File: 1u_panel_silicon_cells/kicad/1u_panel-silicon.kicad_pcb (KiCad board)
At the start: 2 copper layers, 83 x 100 mm, 134 parts, among them J1 MMS-104-01-[F/L]-SH, J2 2-1734592-0, Q1 DMP3050LVT-7, Q2 DMP2240UDM-7, U1 TCAN330GDCNT, U10 TPS63060DSCR, U11 TMP101NA/3KSLOTTED, U12 LTC4412, U13 LTC4411, U14 LTC4411, U15 LTC4411, U16 LTC4411, U2 TMP101NA/3KSLOTTED, U3 LT1618EMSTRPBF, U4 INA226AIDGSR, U5 LTC4411, U6 LTC4411, U7 STM32F091CCT7, U8 LTC4411, U9 LTC4411, X1 ECS-160-10-36Q-ES-TR

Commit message: possibly ready for silicon panel design review?
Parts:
- U13, U14, U15, U16, U5, U6, U8, U9: moved to F.Cu
- moved U14 127.2 mm to (179.8, 119.2), turned to 0 degrees
- moved U15 118.5 mm to (171.2, 105.0), turned to 0 degrees
- moved R31 109.9 mm to (179.5, 116.0)
- moved U13 103.6 mm to (140.8, 117.9), turned to -90 degrees
- moved U8 96.9 mm to (161.0, 96.0)
- moved R32 96.1 mm to (172.2, 101.2)
- moved U16 92.0 mm to (140.5, 104.0)
- moved U9 89.0 mm to (123.1, 118.2), turned to -90 degrees
- moved R28 88.2 mm to (161.0, 98.2), turned to 180 degrees
- moved R30 81.9 mm to (144.5, 117.9), turned to -90 degrees
- moved U6 71.2 mm to (141.2, 89.2)
- moved U5 70.0 mm to (127.8, 92.8), turned to 90 degrees
- moved R29 69.9 mm to (125.8, 118.2), turned to -90 degrees
- moved R8 67.8 mm to (140.8, 91.5), turned to 180 degrees
- moved R33 67.4 mm to (140.5, 106.8), turned to 180 degrees
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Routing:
- net VSOLAR: track 48.2 -> 236.3 mm, vias 12 -> 30
- net Net-(J2-DEBUG-3): track 2.12 -> 89.1 mm
- net Net-(J2-DEBUG-2): track 2.29 -> 88.2 mm
- net Net-(J2-DEBUG-1): track 7.16 -> 92.4 mm
- net Net-(J2-DEBUG-0): track 2.49 -> 86.7 mm
- net Net-(J2-SWO): track 2.38 -> 86.0 mm
- net Net-(J2-VBUSP-Pad1): track 2.08 -> 72.6 mm
- net Net-(D7-A1): track 0.00 -> 17.2 mm, vias 0 -> 4
- net Net-(D8-A1): track 0.00 -> 10.9 mm, vias 0 -> 4
- net Net-(D11-A1): track 0.00 -> 10.6 mm, vias 0 -> 5
- net Net-(D13-A1): track 0.00 -> 7.34 mm, vias 0 -> 5
- net Net-(D12-A1): track 0.00 -> 3.49 mm, vias 0 -> 4
- net Net-(D2-A1): track 0.00 -> 2.98 mm, vias 0 -> 6
- net Net-(D10-A1): track 0.00 -> 2.93 mm, vias 0 -> 5
- net /1u_panel-microcontroller/SWCLK: track 66.0 -> 68.1 mm
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
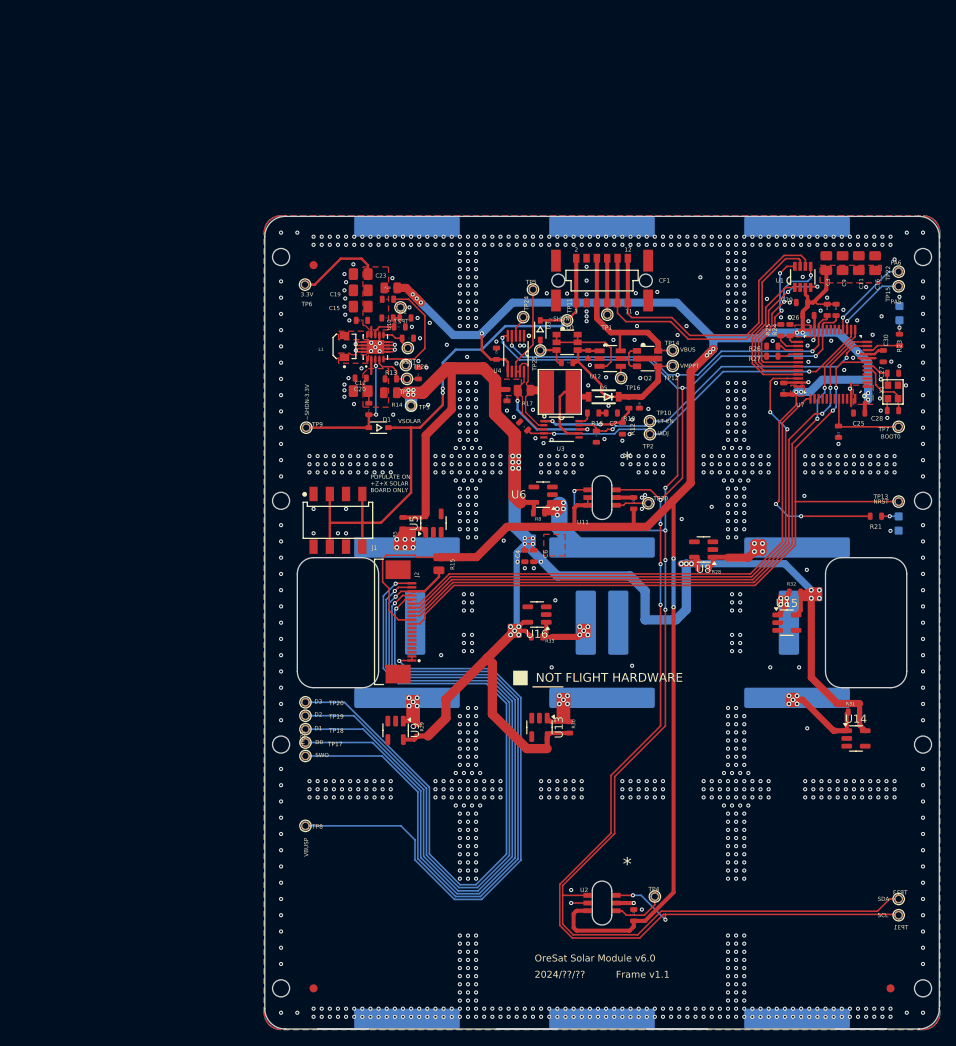
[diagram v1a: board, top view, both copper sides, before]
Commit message: fixed board outline, title blocks
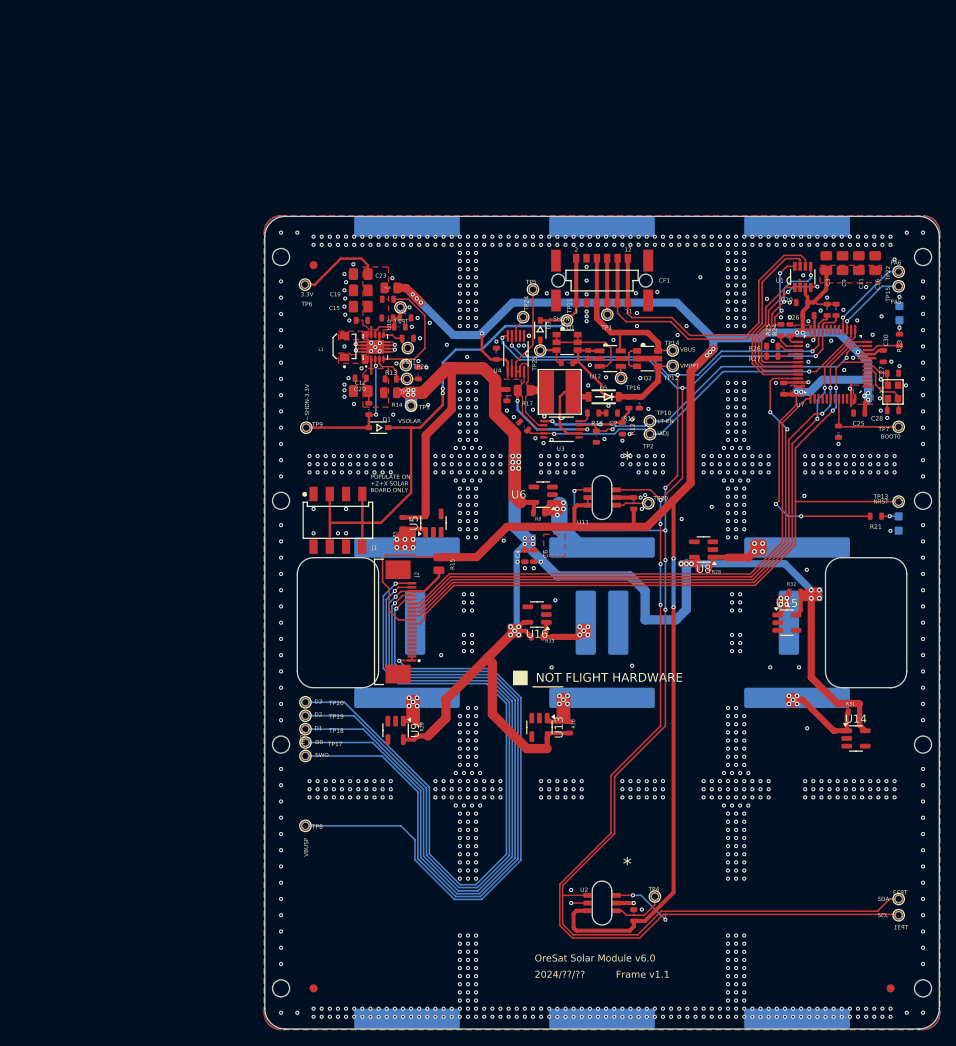
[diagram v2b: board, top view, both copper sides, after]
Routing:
- net GND: track 27.5 -> 31.4 mm
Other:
- outline, holes or cut-outs redrawn

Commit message: updating remote repo for design review
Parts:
- moved R31 0.50 mm to (179.5, 116.5)
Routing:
- net GND: track 31.4 -> 144.6 mm, vias 1180 -> 1202
- net /1u_panel-power/~{SHUTDOWN}: track 75.0 -> 73.1 mm
- net Net-(D11-A1): track 10.6 -> 10.1 mm
- net VSOLAR: track 236.3 -> 236.5 mm, vias 30 -> 28
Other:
- board text added: "2024/08/20"

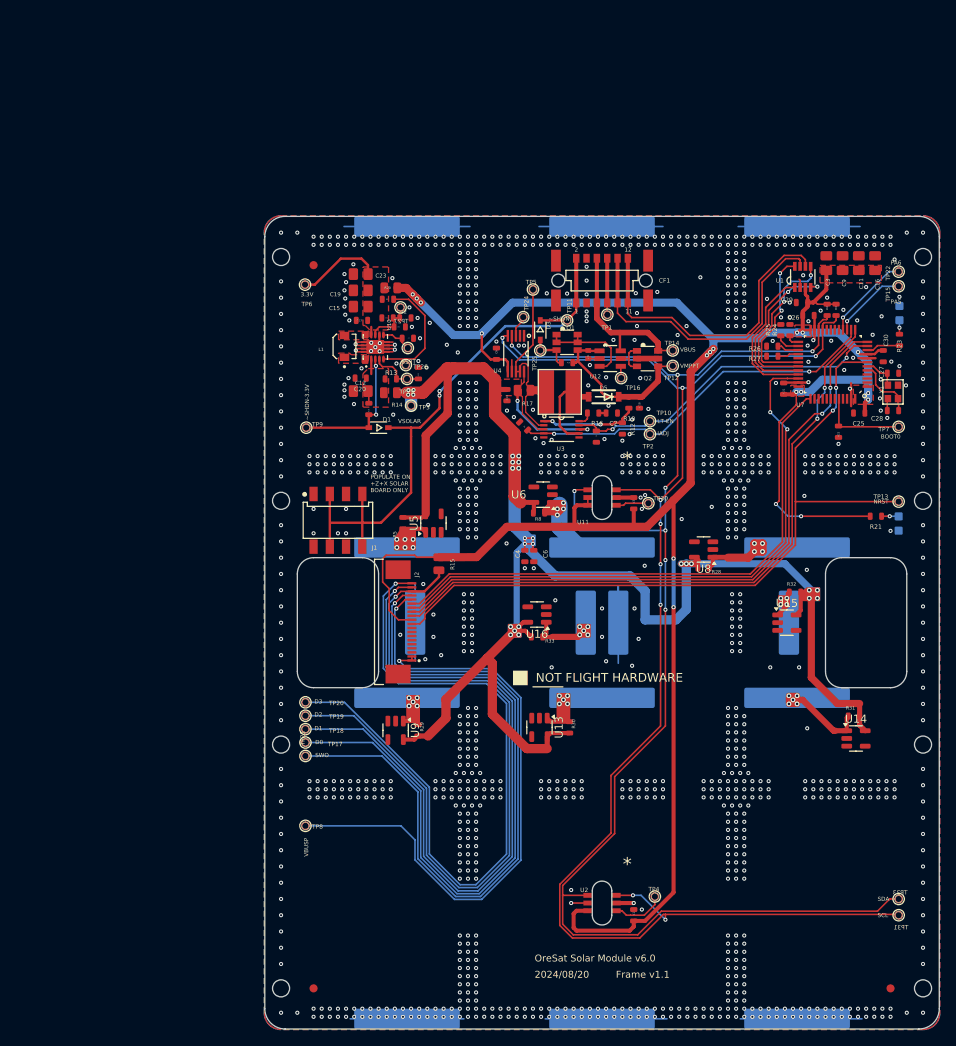
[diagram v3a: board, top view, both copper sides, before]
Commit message: commiting silicon solar panel before moving programming header
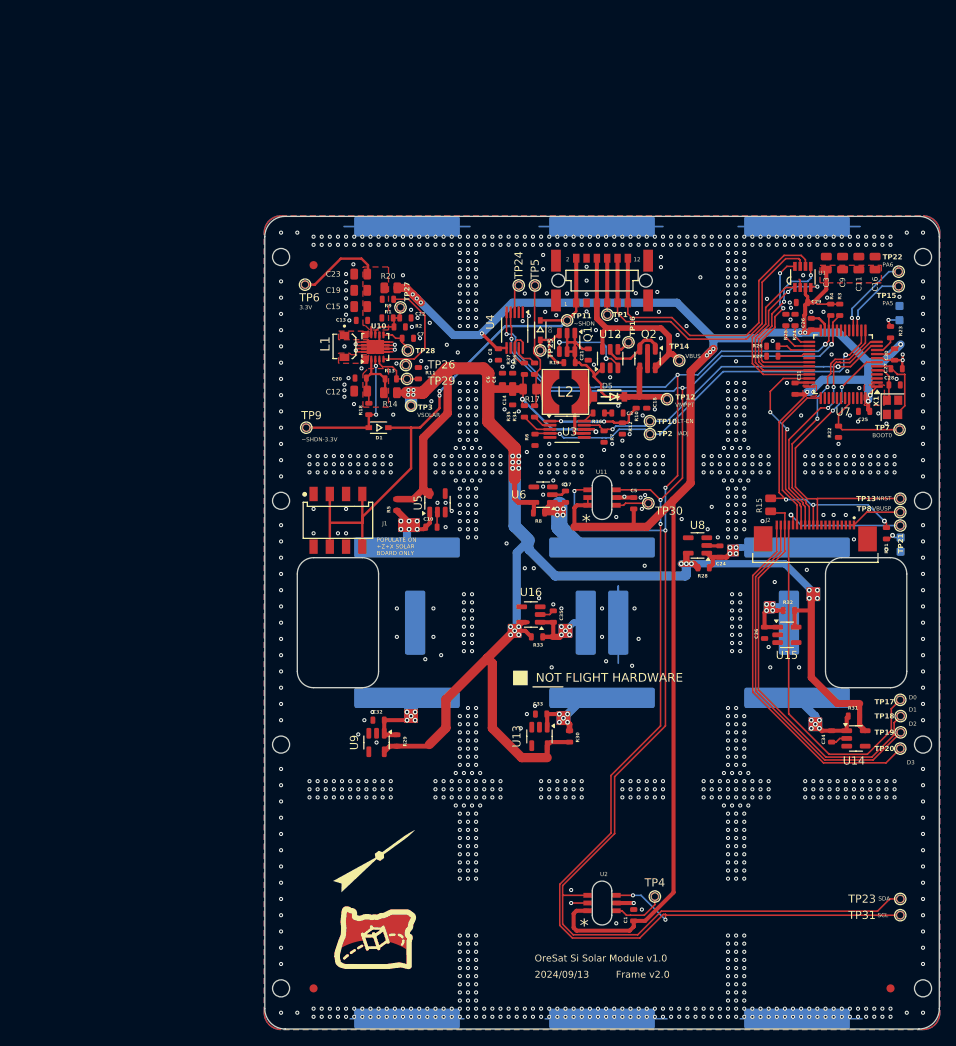
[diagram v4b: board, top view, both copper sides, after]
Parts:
- added C10: 1u, oresat-passives:0603-C-NOSILK, F.Cu at (127.5, 93.2)
- added C17: 1u, oresat-passives:0603-C-NOSILK, F.Cu at (144.0, 89.5)
- added C24: 1u, oresat-passives:0603-C-NOSILK, F.Cu at (163.0, 96.2)
- added C32: 1u, oresat-passives:0603-C-NOSILK, F.Cu at (121.0, 117.0)
- added C33: 1u, oresat-passives:0603-C-NOSILK, F.Cu at (141.0, 116.2)
- added C34: 1u, oresat-passives:0603-C-NOSILK, F.Cu at (176.8, 119.0)
- added C35: 1u, oresat-passives:0603-C-NOSILK, F.Cu at (142.5, 104.2)
- added C36: 1u, oresat-passives:0603-C-NOSILK, F.Cu at (168.5, 106.2)
- added LOGO1: , oresat-graphics:PSAS_LOGO_10X10, F.Cu at (120.8, 134.0)
- added R34: 100, oresat-passives:0603-C-NOSILK, F.Cu at (140.2, 79.0)
- added R35: 100, oresat-passives:0603-C-NOSILK, F.Cu at (138.9, 79.0)
- added R36: 100, oresat-passives:0603-C-NOSILK, F.Cu at (140.2, 73.8)
- added R37: 100, oresat-passives:0603-C-NOSILK, F.Cu at (138.9, 73.8)
- added REF**: logo-small, oresat-graphics:logo-small, F.Cu at (120.5, 143.5)
- C1, C13, C14, C18, C2, C20, C22, C25, C26, C27, C28, C29, C30, C31, C4, C5, C6, C7, C8, R1, R10, R11, R12, R13, R16, R18, R19, R2, R21, R22, R23, R24, R25, R26, R27, R28, R29, R3, R30, R31, R32, R33, R4, R5, R6, R7, R8, R9: footprint 1u_panel:.0603-C-NOSILK -> oresat-passives:0603-C-NOSILK
- C11, C12, C15, C16, C19, C23, C3, C9: footprint 1u_panel:.0805-B-NOSILK -> oresat-passives:0805-C-NOSILK
- C21: footprint 1u_panel:.0402-B-NOSILK -> oresat-passives:0603-C-NOSILK
- CF1: footprint 1u_panel:HARWIN-M55-60X1242R -> oresat-connectors:J-Harwin-M55-60X1242R
- D1, D3: footprint 1u_panel:SOD323-R -> oresat-diodes:D-SOD323-R
- D4, D6: footprint 1u_panel:LED-0603 -> oresat-diodes:LED-0603
- D5: footprint 1u_panel:SOD123 -> oresat-diodes:SOD123
- J1: footprint 1u_panel:SAMTEC-MMS-104-02-X-SH -> oresat-connectors:SAMTEC-MMS-104-02-X-SH
- L1: footprint 1u_panel:IND_1226AS-H-1R0N=P2 -> oresat-passives:IND_1226AS-H-1R0N=P2
- L2: footprint 1u_panel:NONSTANDARD -> oresat-passives:744042100
- PCB1: value ORESAT-SOLAR-BOARD-V4-SPECTROLABS -> ORESAT-SOLAR-BOARD-V1.0-SILICON-CELLS; footprint 1u_panel:ORESAT-SOLAR-BOARD-V4 -> oresat-pcbs:ORESAT-SOLAR-BOARD-V4
- Q1, Q2: footprint 1u_panel:SOT23-6 -> Package_TO_SOT_SMD:SOT-23-6
- R14, R15, R20: footprint 1u_panel:.0805-C-NOSILK -> oresat-passives:0805-C-NOSILK
- R17: value 0.1 0805 -> 0.1; footprint 1u_panel:.0805-C-NOSILK -> oresat-passives:0805-C-NOSILK
- TP1, TP10, TP11, TP12, TP13, TP14, TP15, TP16, TP17, TP18, TP19, TP2, TP20, TP21, TP22, TP23, TP24, TP25, TP26, TP27, TP28, TP29, TP3, TP30, TP31, TP4, TP5, TP6, TP7, TP8, TP9: footprint 1u_panel:1X01 -> oresat-misc:TestPoint-0.75mm-th
- U$1: footprint 1u_panel:FLIGHTMARKER_NEW_BOARDS -> oresat-graphics:FLIGHTMARKER_NEW_BOARDS
- U$2, U$3, U$4: footprint 1u_panel:FIDUCIAL_1MM -> Fiducial:Fiducial_1mm_Mask2mm
- U1: footprint 1u_panel:SOT23-8_TI-DCN -> oresat-ics:SOT23-8_TI-DCN
- U10: footprint 1u_panel:CONV_TPS63060DSCT -> Package_SON:Texas_S-PWSON-N10
- U11, U2: footprint 1u_panel:DBV6-SLOT -> oresat-ics:DBV6-SLOT
- U12: footprint 1u_panel:SOT23-6 -> Package_TO_SOT_SMD:TSOT-23-6
- U3: footprint 1u_panel:MSOP-10_MS -> Package_SO:MSOP-10_3x3mm_P0.5mm
- U4: value INA226AIDGSR -> INA226; footprint 1u_panel:DGS10 -> Package_SO:VSSOP-10_3x3mm_P0.5mm
- U7: footprint 1u_panel:STM32F091C -> Package_QFP:LQFP-48_7x7mm_P0.5mm
- X1: footprint 1u_panel:CRYSTAL_2.5X2 -> Crystal:Crystal_SMD_2520-4Pin_2.5x2.0mm
- moved TP8 82.8 mm to (185.2, 91.4)
- moved TP21 78.5 mm to (185.2, 93.0)
- moved TP20 73.4 mm to (185.2, 120.5), turned to 180 degrees
- moved TP17 73.4 mm to (185.2, 114.5)
- moved TP19 73.3 mm to (185.2, 118.5)
- moved TP18 73.3 mm to (185.2, 116.5)
- moved J2 52.4 mm to (174.8, 94.7), turned to 180 degrees
- moved R15 41.5 mm to (169.2, 90.5), turned to 90 degrees
- moved C6 22.1 mm to (136.2, 75.0), turned to 90 degrees
- moved C4 21.9 mm to (137.5, 75.0), turned to 90 degrees
- moved TP16 4.49 mm to (151.8, 70.5)
- moved TP12 4.16 mm to (156.5, 77.5)
- moved TP24 3.94 mm to (138.2, 63.5)
- moved C28 3.16 mm to (184.5, 75.8), turned to 0 degrees
- moved U4 2.91 mm to (137.8, 69.0)
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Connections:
- net Net-(U7-PF0-OSC_IN) renamed /1u_panel-microcontroller/OSC_IN
- net Net-(U7-PF1-OSC_OUT) renamed /1u_panel-microcontroller/OSC_OUT
- L1 pad 1: Net-(U10-L1) -> Net-(U10-L2)
- L1 pad 2: Net-(U10-L2) -> Net-(U10-L1)
- Q1 pad 1: Net-(U12-CTL) -> /1u_panel-power/VMPPT
- Q1 pad 2: Net-(U12-CTL) -> /1u_panel-power/VMPPT
- Q1 pad 4: /1u_panel-power/VMPPT -> Net-(Q1-S)
- Q1 pad 5: Net-(U12-CTL) -> /1u_panel-power/VMPPT
- Q1 pad 6: Net-(U12-CTL) -> /1u_panel-power/VMPPT
- R15 pad 1: 3.3V -> Net-(J2-DEBUG-1)
- R15 pad 2: Net-(J2-DEBUG-1) -> 3.3V
- R17 pad 2: Net-(L2-1) -> Net-(L2-Pad1)
- R18 pad 1: Net-(U10-VIN) -> /1u_panel-power/~{SHDN-3.3V}
- R18 pad 2: /1u_panel-power/~{SHDN-3.3V} -> Net-(U10-VIN)
- R7 pad 1: GND -> LT1618-ENABLE
- R7 pad 2: LT1618-ENABLE -> GND
- TP5 pad 1: Net-(L2-1) -> Net-(L2-Pad1)
- U12 pad 3: Net-(U12-CTL) -> Net-(Q1-S)
- U3 pad 2: Net-(L2-1) -> Net-(U3-ISN)
- U3 pad 3: VSOLAR -> Net-(U3-ISP)
- U4 pad 10: VSOLAR -> Net-(U4-Vbus)
- U4 pad 4: SDA -> SCL
- U4 pad 5: SCL -> SDA
- U4 pad 8: Net-(L2-1) -> Net-(U4-Vbus)
- U4 pad 9: Net-(L2-1) -> Net-(U4-Vin-)
- X1 pad 4: GND -> (no net)
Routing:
- net Net-(J2-SWO): track 86.0 -> 15.3 mm
- net Net-(J2-VBUSP-Pad1): track 72.6 -> 6.86 mm, vias 1 -> 0
- net /1u_panel-microcontroller/NRESET: track 92.2 -> 37.0 mm
- net /1u_panel-microcontroller/PA3/USART2_RX: track 80.1 -> 29.6 mm
- net /1u_panel-microcontroller/PA2/USART2_TX: track 80.2 -> 29.9 mm
- net /1u_panel-microcontroller/SWDIO: track 73.7 -> 23.6 mm
- net /1u_panel-microcontroller/SWCLK: track 68.1 -> 19.3 mm
- net Net-(J2-DEBUG-3): track 89.1 -> 44.3 mm, vias 1 -> 0
- net Net-(J2-DEBUG-1): track 92.4 -> 48.6 mm, vias 1 -> 0
- net Net-(J2-DEBUG-2): track 88.2 -> 44.5 mm, vias 1 -> 0
- net Net-(J2-DEBUG-0): track 86.7 -> 43.4 mm, vias 1 -> 0
- net 3.3V: track 287.3 -> 261.6 mm, vias 18 -> 17
- net Net-(L2-1): track 24.5 -> 0.00 mm
- net Net-(L2-Pad1): track 0.00 -> 15.6 mm
- net Net-(U12-CTL): track 12.2 -> 0.00 mm
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- removed copper zone on F.Cu, net VSOLAR
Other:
- board text added: "2024/09/13"
- board text added: "NOTE: See User.Draiwings layer for component placement restrictions -> <0.7mm component height in circles"
- board text added: "OreSat Si Solar Module v1.0"
- board text added: "OreSat Si-Solar Module v1.0"
- board text removed: "2024/08/20"
- board text removed: "2024/??/??"
- board text removed: "Frame v1.1"
- board text removed: "NOTE: See DXF layer for component placement restrictions"
- board text removed: "OreSat Solar Module v6.0"
- board text removed: "PA0"
- board text removed: "SDO"
